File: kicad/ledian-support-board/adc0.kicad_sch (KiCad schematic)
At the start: 21 parts, among them U3 MCP3208, U9 REF3030

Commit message: kicad: ledian-support-board: added titles to all pages
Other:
- title: (none) -> ADC0
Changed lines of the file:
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@@
 (kicad_sch (version 20230121) (generator eeschema)
   (paper "A4")
+  (title_block
+    (title "ADC0")
+  )
   (junction (at 184.15 102.87) (diameter 0) (color 0 0 0 0)
   )

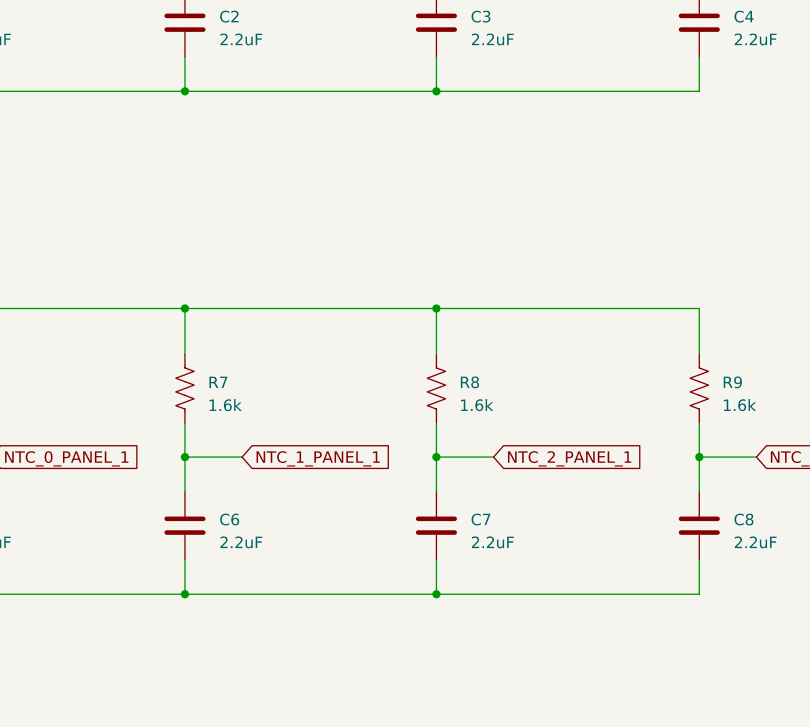
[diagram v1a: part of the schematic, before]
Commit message: kicad: ledian-support-board: added some comments to parts of the circuit
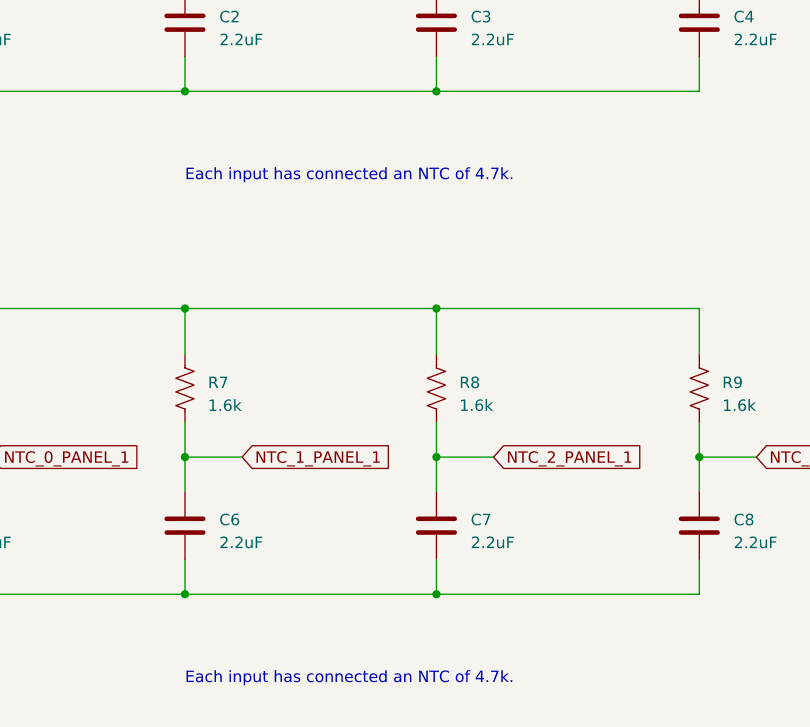
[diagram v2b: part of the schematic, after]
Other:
- note added: "Each input has connected an NTC of 4.7k."
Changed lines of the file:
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@@
     (stroke (width 0) (type default))
+  )
+  (text "Each input has connected an NTC of 4.7k." (at 184.15 144.78 0)
+    (effects (font (size 1.27 1.27)) (justify left bottom))
+  )
+  (text "Each input has connected an NTC of 4.7k." (at 184.15 88.9 0)
+    (effects (font (size 1.27 1.27)) (justify left bottom))
   )
   (global_label "NTC_0_PANEL_1" (shape input) (at 91.44 71.12 0) (fields_autoplaced)
